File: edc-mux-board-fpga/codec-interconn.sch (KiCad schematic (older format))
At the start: 0 parts

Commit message: starting to work on mezzanine board interconnections.
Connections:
- no-connect marks 32 -> 30
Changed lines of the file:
@@
 $Descr USLedger 11000 17000 portrait
 encoding utf-8
-Sheet 4 25
+Sheet 4 28
 Title ""
 Date ""
@@
 F6 "WCLK" O R 3650 2000 50
 F7 "~RESET" I R 3650 2100 50
-F8 "GPI" I R 3650 2200 50
-F9 "SCL" I L 2100 1600 50
-F10 "SDA" B L 2100 1700 50
-F11 "INT1_OUT" O R 3650 2400 50
-F12 "ID_PIN" O L 2100 2500 50
+F8 "SCL" I L 2100 1600 50
+F9 "SDA" B L 2100 1700 50
 $EndSheet
 $Sheet
@@
 F10 "SDA" B L 2100 3200 50
 F11 "INT1_OUT" O R 3650 3900 50
-F12 "ID_PIN" O L 2100 4000 50
 $EndSheet
 $Sheet
@@
 Text Label 2000 12400 2    50   ~ 0
 MCLK7
-Text Label 2000 2500 2    50   ~ 0
-ID_PIN0
-Text Label 2000 4000 2    50   ~ 0
-ID_PIN1
 Text Label 2000 5500 2    50   ~ 0
 ID_PIN2
@@
 ID_PIN15
 Entry Wire Line
-	1600 4100 1700 4000
-Entry Wire Line
 	1600 5600 1700 5500
 Entry Wire Line
@@
 	1600 13100 1700 13000
 Wire Wire Line
-	1700 2500 2100 2500
-Wire Wire Line
-	1700 4000 2100 4000
-Wire Wire Line
 	1700 5500 2100 5500
 Wire Wire Line
@@
 Wire Wire Line
 	1700 13000 2100 13000
-Entry Wire Line
-	1600 2600 1700 2500
 Text Label 1600 13650 1    50   ~ 0
 ID_PIN[0..7]
@@
 Text Label 7200 12500 2    50   ~ 0
 WCLK15
-NoConn ~ 3650 2400
 NoConn ~ 3650 3900
 NoConn ~ 3650 5400
@@
 Text Label 7200 12600 2    50   ~ 0
 ~RESET~15
-NoConn ~ 3650 2200
 NoConn ~ 3650 3700
 NoConn ~ 3650 5200
@@
 	6050 900  6550 900
 Wire Bus Line
+	6050 1000 6350 1000
+Wire Bus Line
 	5050 1250 5050 13000
 Wire Bus Line
@@
 	1300 2000 1300 14150
 Wire Bus Line
-	1600 2600 1600 13700
-Wire Bus Line
 	5950 1700 5950 13000
-Wire Bus Line
-	6050 1000 6350 1000
 $EndSCHEMATC

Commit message: Finished Codec Interconnect Busses
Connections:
- no-connect marks 30 -> 0

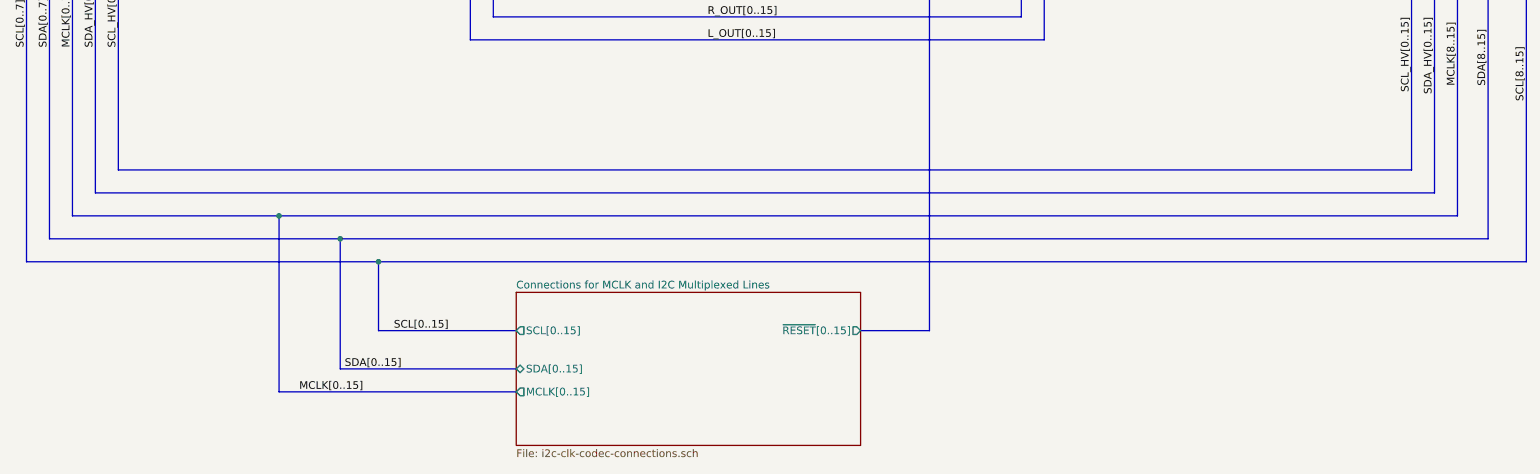
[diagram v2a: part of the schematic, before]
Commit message: Finished CODEC and MCU interconnections
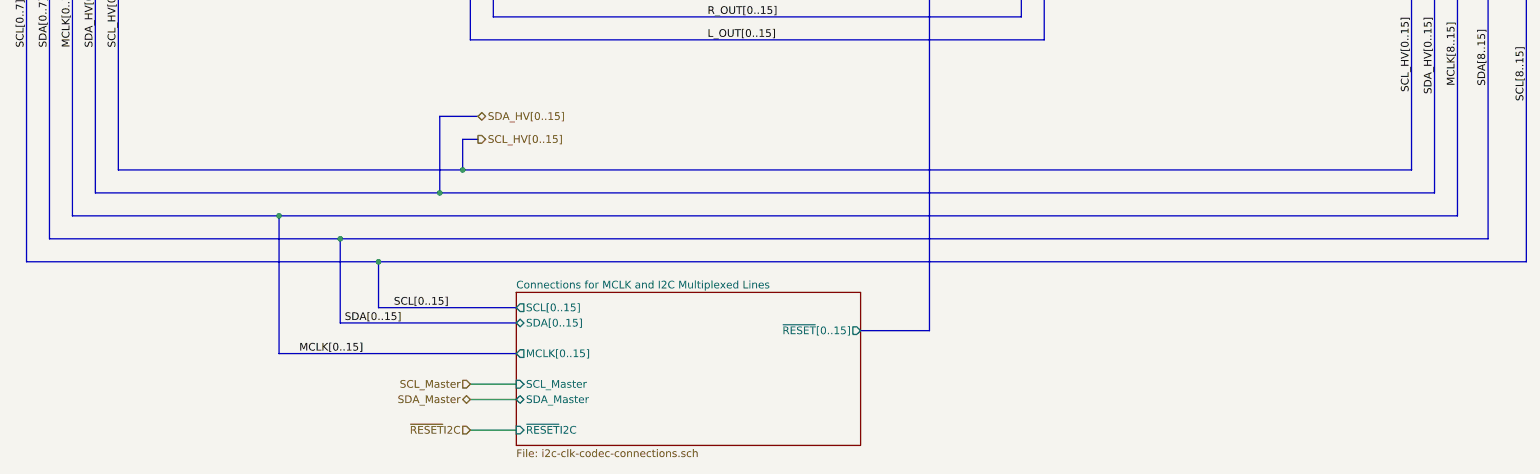
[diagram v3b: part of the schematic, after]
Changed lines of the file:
@@
 F0 "Connections for MCLK and I2C Multiplexed Lines" 50
 F1 "i2c-clk-codec-connections.sch" 50
-F2 "SCL[0..15]" O L 3800 15400 50
-F3 "SDA[0..15]" B L 3800 15650 50
-F4 "MCLK[0..15]" O L 3800 15800 50
+F2 "SCL[0..15]" O L 3800 15250 50
+F3 "SDA[0..15]" B L 3800 15350 50
+F4 "MCLK[0..15]" O L 3800 15550 50
 F5 "~RESET~[0..15]" O R 6050 15400 50
+F6 "SCL_Master" I L 3800 15750 50
+F7 "SDA_Master" B L 3800 15850 50
+F8 "~RESET~I2C" I L 3800 16050 50
 $EndSheet
 Wire Bus Line
@@
 	750  14800 2650 14800
 Wire Bus Line
-	2900 14950 2900 15400
+	2900 14950 2900 15250
 Connection ~ 2900 14950
 Wire Bus Line
 	2900 14950 10400 14950
-Text Label 3000 15400 0    50   ~ 0
+Text Label 3000 15250 0    50   ~ 0
 SCL[0..15]
 Wire Bus Line
-	2650 14800 2650 15650
-Wire Bus Line
-	2650 15650 3800 15650
+	2650 14800 2650 15350
+Wire Bus Line
+	2650 15350 3800 15350
 Connection ~ 2650 14800
 Wire Bus Line
 	2650 14800 10150 14800
-Text Label 3050 15650 2    50   ~ 0
+Text Label 3050 15350 2    50   ~ 0
 SDA[0..15]
 Wire Bus Line
-	2250 15800 3800 15800
-Text Label 2800 15800 2    50   ~ 0
+	2250 15550 3800 15550
+Text Label 2800 15550 2    50   ~ 0
 MCLK[0..15]
 Text Label 3050 1400 0    50   ~ 0
@@
 	7250 2500 7350 2400
 Wire Bus Line
-	2900 15400 3800 15400
+	2900 15250 3800 15250
 Entry Wire Line
 	9700 1900 9800 2000
@@
 	600  14950 2900 14950
 Wire Bus Line
-	2250 15800 2250 14650
+	2250 15550 2250 14650
 Connection ~ 2250 14650
 Wire Bus Line
 	2250 14650 9950 14650
 Wire Bus Line
-	1050 14500 9800 14500
-Wire Bus Line
-	9650 14350 1200 14350
+	1050 14500 3300 14500
+Wire Bus Line
+	9650 14350 3450 14350
 Text Label 9650 13350 3    50   ~ 0
 SCL_HV[0..15]
@@
 Text Label 5050 13500 0    50   ~ 0
 L_OUT[0..15]
+Text HLabel 3500 15750 0    50   Input ~ 0
+SCL_Master
+Text HLabel 3500 15850 0    50   BiDi ~ 0
+SDA_Master
+Text HLabel 3500 16050 0    50   Input ~ 0
+~RESET~I2C
+Wire Wire Line
+	3500 15750 3800 15750
+Wire Wire Line
+	3500 15850 3800 15850
+Wire Wire Line
+	3500 16050 3800 16050
+Text HLabel 3550 14000 2    50   BiDi ~ 0
+SDA_HV[0..15]
+Wire Bus Line
+	3300 14500 3300 14000
+Wire Bus Line
+	3300 14000 3550 14000
+Connection ~ 3300 14500
+Wire Bus Line
+	3300 14500 9800 14500
+Text HLabel 3550 14150 2    50   Output ~ 0
+SCL_HV[0..15]
+Wire Bus Line
+	3450 14350 3450 14150
+Wire Bus Line
+	3450 14150 3550 14150
+Connection ~ 3450 14350
+Wire Bus Line
+	3450 14350 1200 14350
 Wire Bus Line
 	9800 2000 9800 14500

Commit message: Finished FPGA and MCU interconnections.
Finished up interrupt wiring
Fixed a few missing connections
Annotated Schematic
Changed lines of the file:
@@
 Wire Bus Line
 	3500 2500 3500 13500
+Text Label 3050 2000 0    50   ~ 0
+L_IN0
+Text Label 3050 3500 0    50   ~ 0
+L_IN1
+Text Label 3050 5000 0    50   ~ 0
+L_IN2
+Text Label 3050 6500 0    50   ~ 0
+L_IN3
+Text Label 3050 8000 0    50   ~ 0
+L_IN4
+Text Label 3050 9500 0    50   ~ 0
+L_IN5
+Text Label 3050 11000 0    50   ~ 0
+L_IN6
+Text Label 3050 12500 0    50   ~ 0
+L_IN7
+Text Label 3050 2100 0    50   ~ 0
+R_IN0
+Text Label 3050 3600 0    50   ~ 0
+R_IN1
+Text Label 3050 5100 0    50   ~ 0
+R_IN2
+Text Label 3050 6600 0    50   ~ 0
+R_IN3
+Text Label 3050 8100 0    50   ~ 0
+R_IN4
+Text Label 3050 9600 0    50   ~ 0
+R_IN5
+Text Label 3050 11100 0    50   ~ 0
+R_IN6
+Text Label 3050 12600 0    50   ~ 0
+R_IN7
+Text Label 3050 2200 0    50   ~ 0
+AUD_GND0
+Text Label 3050 3700 0    50   ~ 0
+AUD_GND1
+Text Label 3050 5200 0    50   ~ 0
+AUD_GND2
+Text Label 3050 6700 0    50   ~ 0
+AUD_GND3
+Text Label 3050 8200 0    50   ~ 0
+AUD_GND4
+Text Label 3050 9700 0    50   ~ 0
+AUD_GND5
+Text Label 3050 11200 0    50   ~ 0
+AUD_GND6
+Text Label 3050 12700 0    50   ~ 0
+AUD_GND7
+Text Label 3050 2300 0    50   ~ 0
+R_OUT0
+Text Label 3050 3800 0    50   ~ 0
+R_OUT1
+Text Label 3050 5300 0    50   ~ 0
+R_OUT2
+Text Label 3050 6800 0    50   ~ 0
+R_OUT3
+Text Label 3050 8300 0    50   ~ 0
+R_OUT4
+Text Label 3050 9800 0    50   ~ 0
+R_OUT5
+Text Label 3050 11300 0    50   ~ 0
+R_OUT6
+Text Label 3050 12800 0    50   ~ 0
+R_OUT7
+Text Label 3050 2400 0    50   ~ 0
+L_OUT0
+Text Label 3050 3900 0    50   ~ 0
+L_OUT1
+Text Label 3050 5400 0    50   ~ 0
+L_OUT2
+Text Label 3050 6900 0    50   ~ 0
+L_OUT3
+Text Label 3050 8400 0    50   ~ 0
+L_OUT4
+Text Label 3050 9900 0    50   ~ 0
+L_OUT5
+Text Label 3050 11400 0    50   ~ 0
+L_OUT6
+Text Label 3050 12900 0    50   ~ 0
+L_OUT7
 $EndSCHEMATC
